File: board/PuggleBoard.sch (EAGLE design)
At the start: 129 parts, among them U1 OPA4209, U10 24C, U2 ADS8331, U3 AD5686, U4 OPA4209, U5 LM2663, U6 TPS7A3001, U7 TPS7A4901, U8 REF5040, U9 AD8032

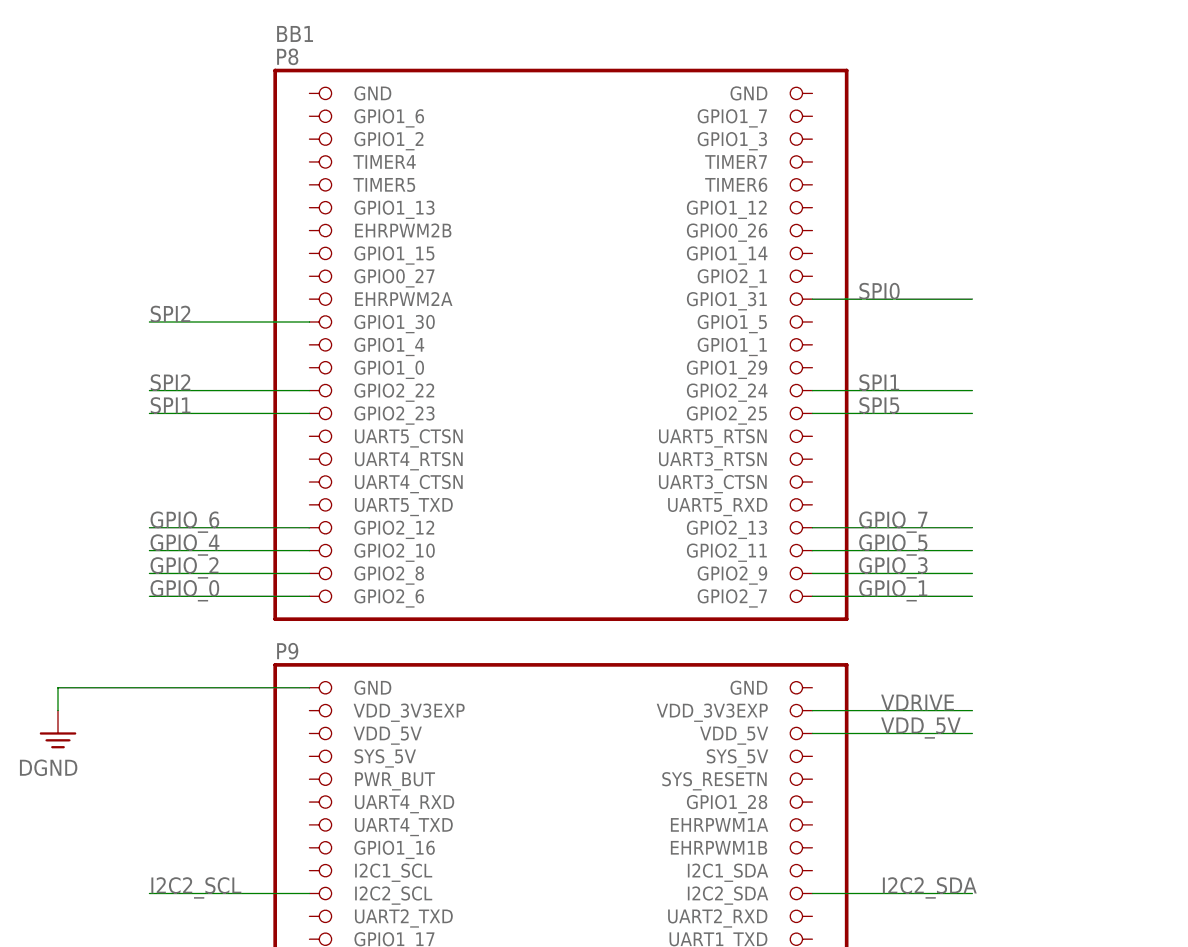
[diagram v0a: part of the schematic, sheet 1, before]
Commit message: Trying to get the positions of the ground planes optimal.
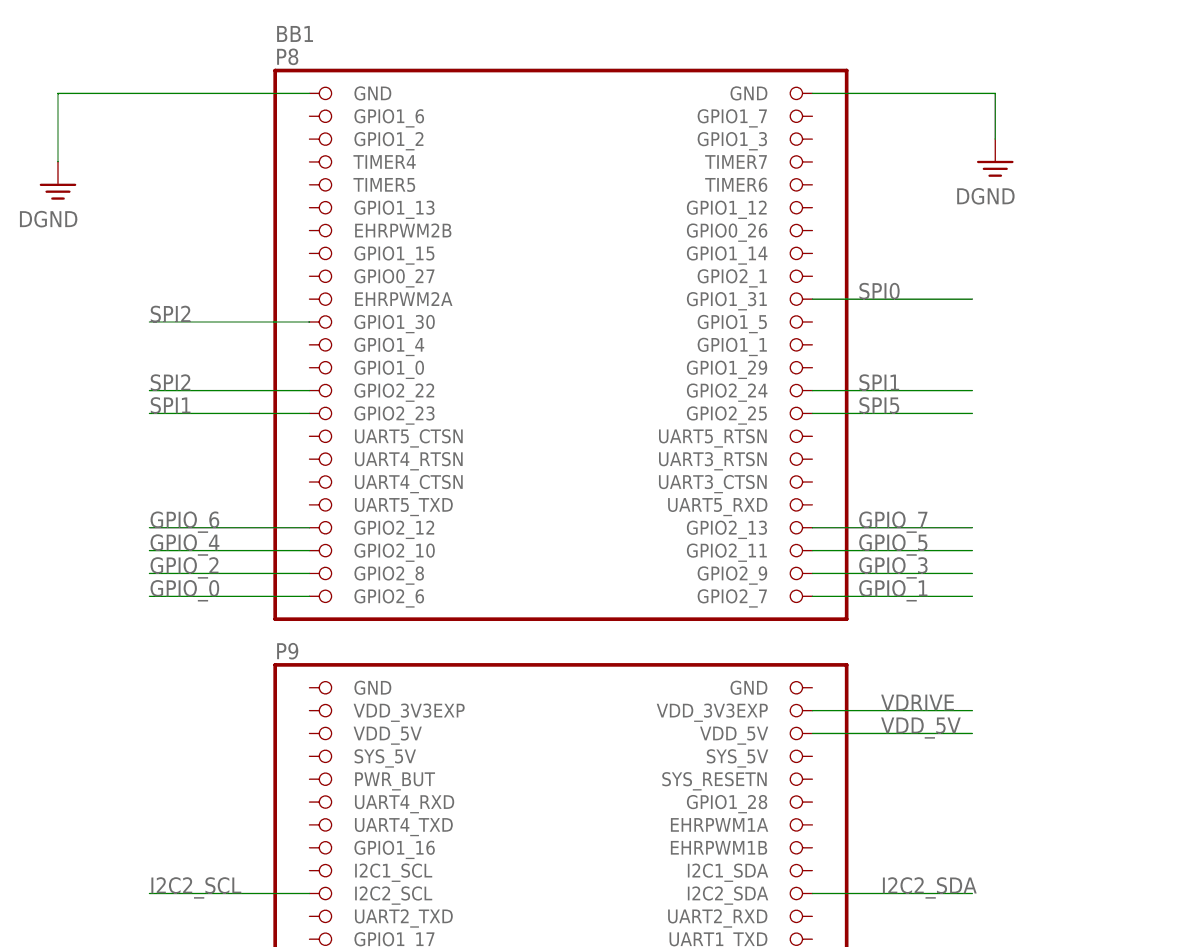
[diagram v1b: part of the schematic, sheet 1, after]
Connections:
- net DGND: now also BB1.GND@7, BB1.GND@8; no longer BB1.GND@1
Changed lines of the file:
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@@
 <part name="C43" library="rcl" deviceset="C-EU" device="C0603" value="0.1uF"/>
 <part name="C44" library="rcl" deviceset="C-EU" device="C0603" value="0.1uF"/>
+<part name="DGND3" library="supply2" deviceset="PE" device="" value="DGND"/>
 </parts>
 <sheets>
@@
 <instances>
 <instance part="BB1" gate="G$1" x="-35.56" y="48.26"/>
-<instance part="DGND2" gate="PE" x="-91.44" y="38.1"/>
+<instance part="DGND2" gate="PE" x="-91.44" y="99.06"/>
 <instance part="A_I/O" gate="G$1" x="53.34" y="50.8"/>
 <instance part="PWR_EXT" gate="A" x="53.34" y="0"/>
@@
 <instance part="DGND10" gate="PE" x="60.96" y="-27.94"/>
 <instance part="A_I/O1" gate="G$1" x="53.34" y="27.94"/>
+<instance part="DGND3" gate="PE" x="12.7" y="101.6"/>
 </instances>
 <busses>
@@
 <segment>
 <pinref part="DGND2" gate="PE" pin="PE"/>
-<wire x1="-91.44" y1="40.64" x2="-91.44" y2="43.18" width="0.1524" layer="91"/>
-<pinref part="BB1" gate="G$1" pin="GND@1"/>
-<wire x1="-91.44" y1="43.18" x2="-63.5" y2="43.18" width="0.1524" layer="91"/>
+<wire x1="-91.44" y1="101.6" x2="-91.44" y2="109.22" width="0.1524" layer="91"/>
+<pinref part="BB1" gate="G$1" pin="GND@7"/>
+<wire x1="-91.44" y1="109.22" x2="-63.5" y2="109.22" width="0.1524" layer="91"/>
 </segment>
 <segment>
@@
 <wire x1="58.42" y1="30.48" x2="73.66" y2="30.48" width="0.1524" layer="91"/>
 <label x="66.04" y="30.48" size="1.778" layer="95"/>
+</segment>
+<segment>
+<pinref part="BB1" gate="G$1" pin="GND@8"/>
+<wire x1="-7.62" y1="109.22" x2="12.7" y2="109.22" width="0.1524" layer="91"/>
+<wire x1="12.7" y1="109.22" x2="12.7" y2="104.14" width="0.1524" layer="91"/>
+<pinref part="DGND3" gate="PE" pin="PE"/>
 </segment>
 </net>
@@
 <wire x1="111.76" y1="-33.02" x2="129.54" y2="-33.02" width="0.1524" layer="91"/>
 <junction x="111.76" y="-33.02"/>
-</segment>
-</net>
+<junction x="129.54" y="-33.02"/>
+</segment>
+</net>

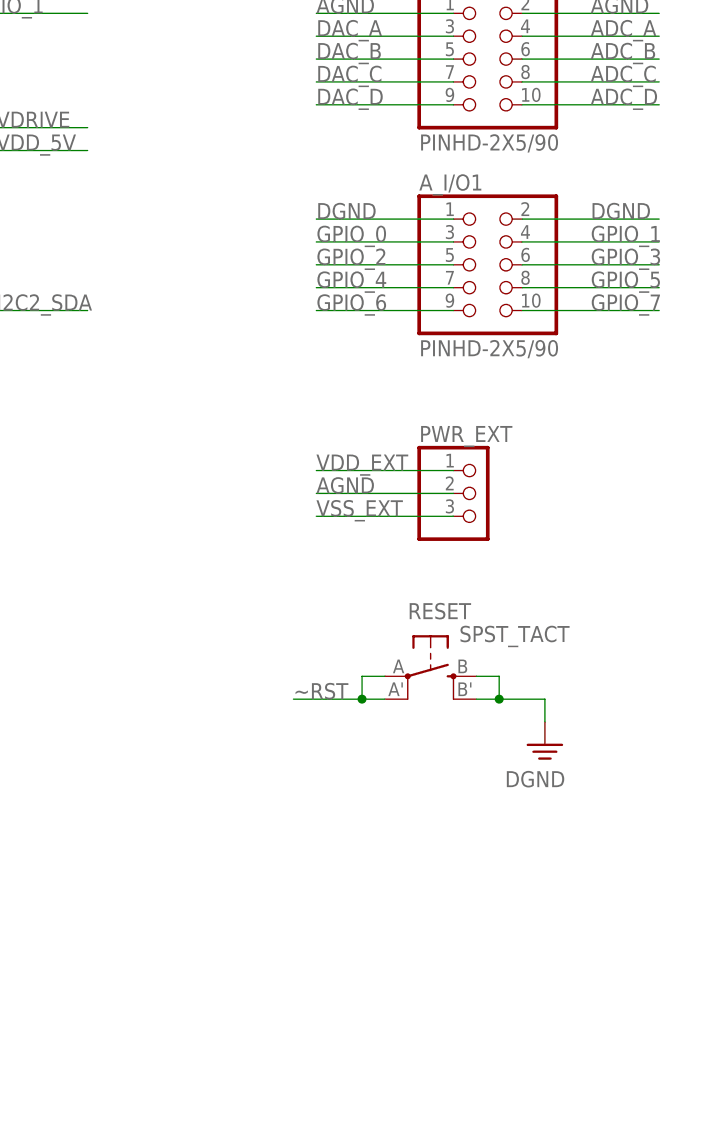
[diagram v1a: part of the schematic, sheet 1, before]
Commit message: Relaced through-hole header for GPIO with HDMI connector. This board will be intan ready.
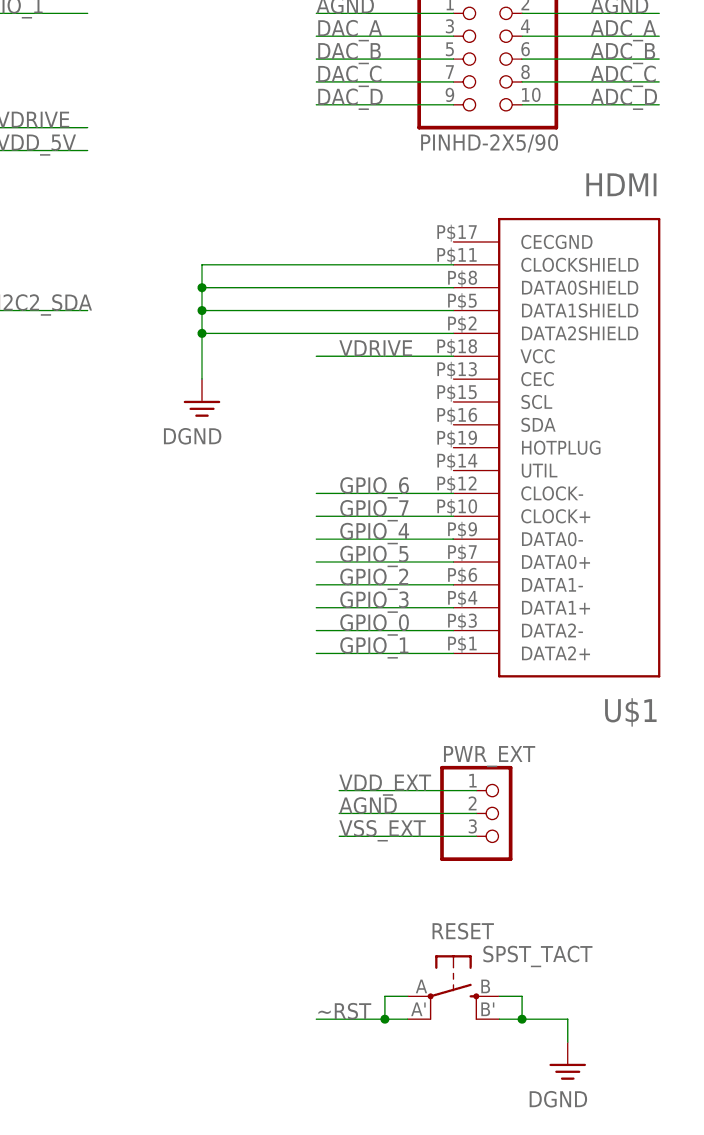
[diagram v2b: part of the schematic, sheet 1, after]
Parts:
- removed A_I/O1: PINHD-2X5/90, adafruit:PINHD-2X5/90
- added U$1: HDMI, open-ephys:HDMI
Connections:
- net DGND: now also U$1.CLOCKSHIELD, U$1.DATA0SHIELD, U$1.DATA1SHIELD, U$1.DATA2SHIELD; no longer A_I/O1.1, A_I/O1.2
- net GPIO_0: now also U$1.DATA2-; no longer A_I/O1.3
- net GPIO_1: now also U$1.DATA2+; no longer A_I/O1.4
- net GPIO_2: now also U$1.DATA1-; no longer A_I/O1.5
- net GPIO_3: now also U$1.DATA1+; no longer A_I/O1.6
- net GPIO_4: now also U$1.DATA0-; no longer A_I/O1.7
- net GPIO_5: now also U$1.DATA0+; no longer A_I/O1.8
- net GPIO_6: now also U$1.CLOCK-; no longer A_I/O1.9
- net GPIO_7: now also U$1.CLOCK+; no longer A_I/O1.10
- net VDRIVE: now also U$1.VCC
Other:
- moved on the sheet: PWR_EXT, RESET

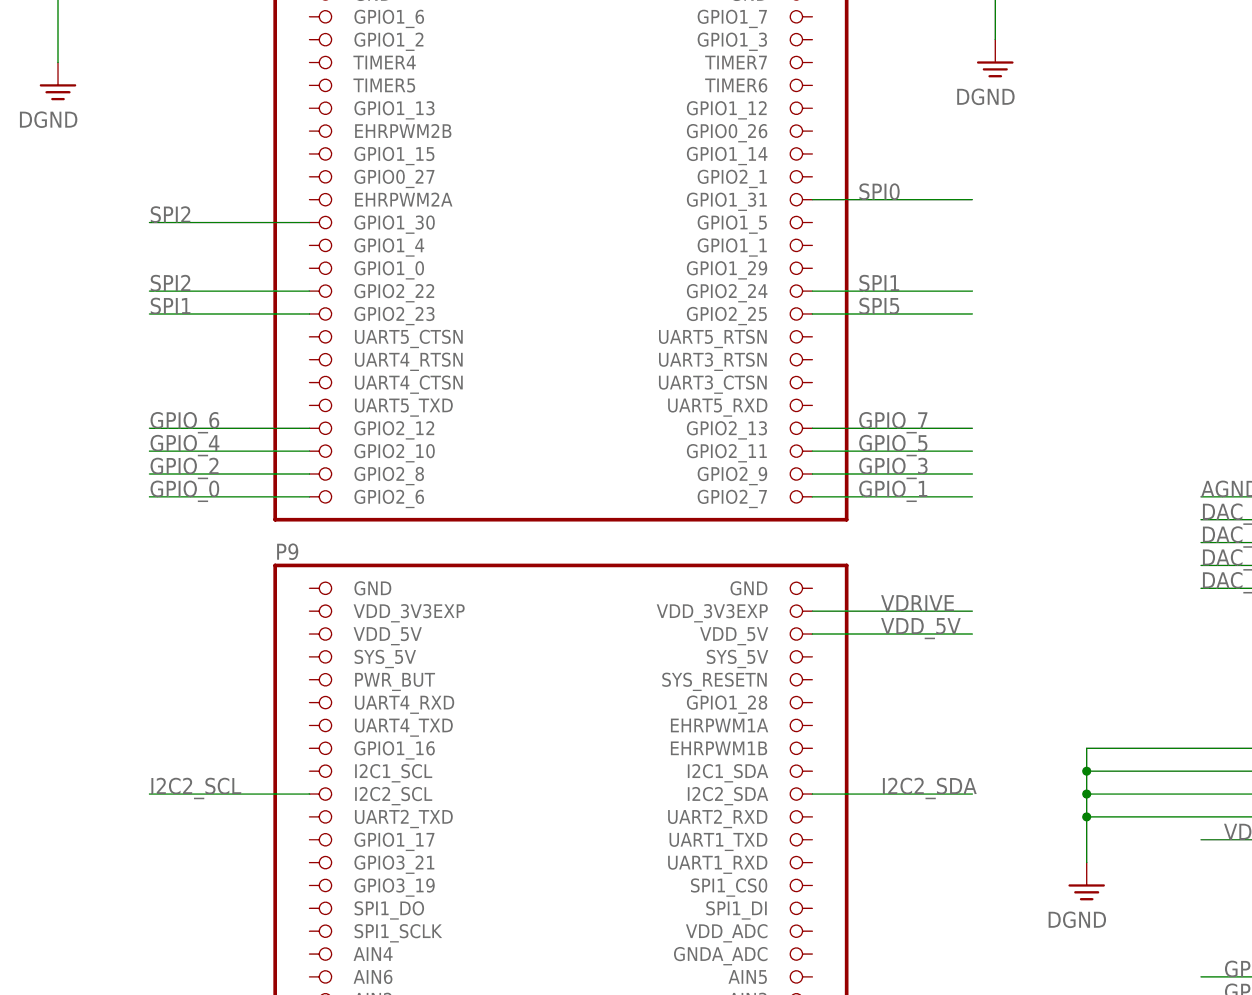
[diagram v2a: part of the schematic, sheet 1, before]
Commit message: Added series resistors to digital I/O lines.
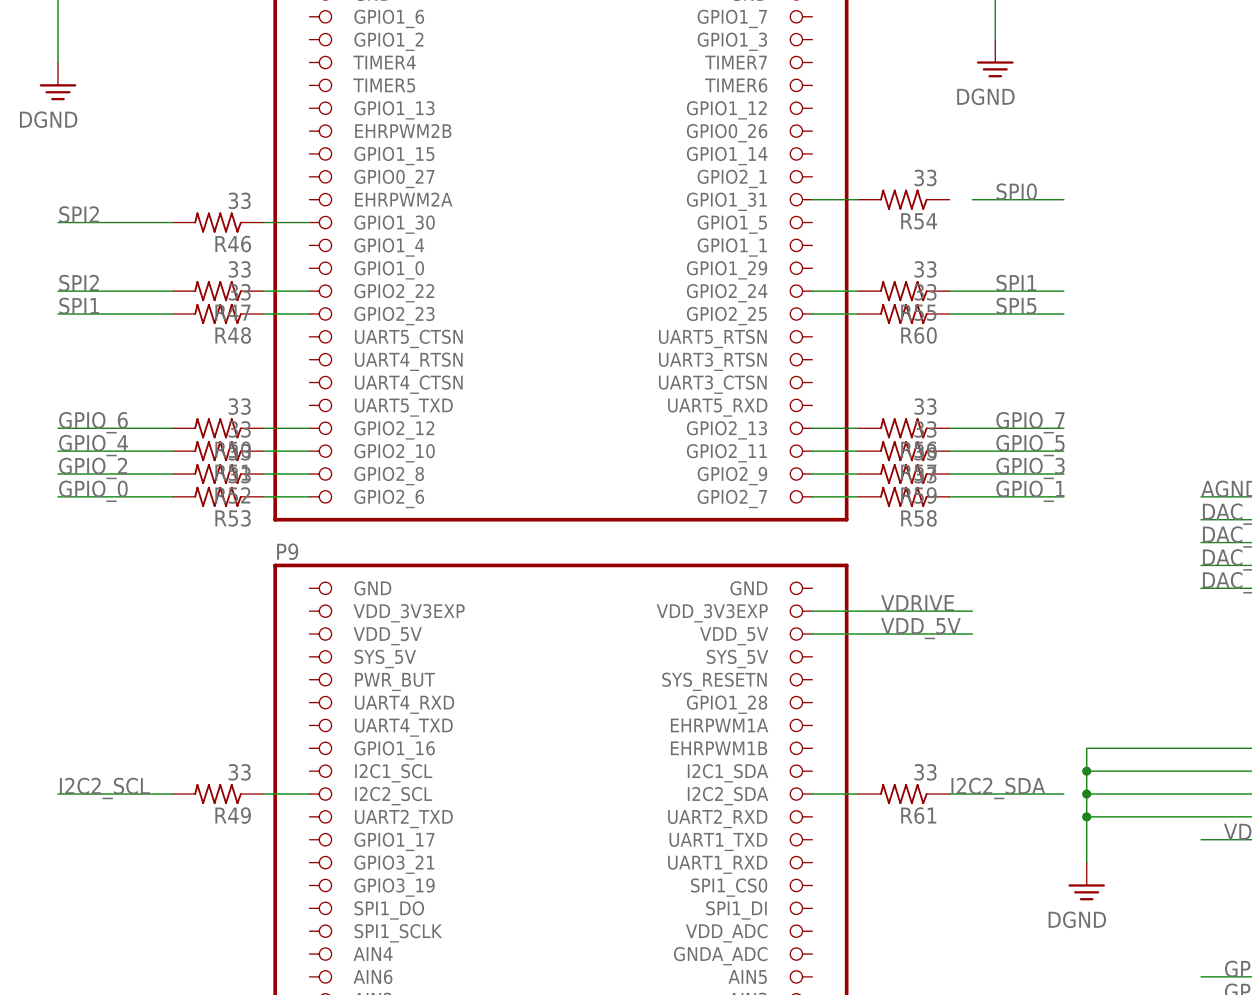
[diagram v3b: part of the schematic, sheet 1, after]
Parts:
- added R46, R47, R48, R49, R50, R51, R52, R53, R54, R55, R56, R57, R58, R59, R60, R61: 33, rcl:R-US_R0603
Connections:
- removed net SPI0: BB1.GPIO1_31, U2.FS/~CS
- removed net SPI3: U2.SDI, U3.SDIN
- removed net SPI4: U2.SDO, U3.SDO
- new net N$10: BB1.GPIO2_24, R55.2
- new net N$12: BB1.GPIO1_31, R54.2
- new net N$13: BB1.GPIO2_13, R56.2
- new net N$15: BB1.GPIO2_11, R57.2
- new net N$17: BB1.GPIO2_9, R59.2
- new net N$21: BB1.GPIO2_7, R58.2
- new net N$23: BB1.GPIO2_6, R53.1
- new net N$25: BB1.GPIO2_8, R52.1
- new net N$26: BB1.GPIO2_10, R51.1
- new net N$27: BB1.GPIO2_12, R50.1
- new net N$28: BB1.GPIO2_23, R48.1
- new net N$29: BB1.GPIO2_22, R47.1
- new net N$30: BB1.GPIO1_30, R46.1
- new net N$31: BB1.I2C2_SCL, R49.1
- new net N$35: BB1.I2C2_SDA, R61.2
- new net N$8: BB1.GPIO2_25, R60.2
- net GPIO_0: now also R53.2; no longer BB1.GPIO2_6
- net GPIO_1: now also R58.1; no longer BB1.GPIO2_7
- net GPIO_2: now also R52.2; no longer BB1.GPIO2_8
- net GPIO_3: now also R59.1; no longer BB1.GPIO2_9
- net GPIO_4: now also R51.2; no longer BB1.GPIO2_10
- net GPIO_5: now also R57.1; no longer BB1.GPIO2_11
- net GPIO_6: now also R50.2; no longer BB1.GPIO2_12
- net GPIO_7: now also R56.1; no longer BB1.GPIO2_13
- net I2C2_SCL: no longer BB1.I2C2_SCL
- net I2C2_SDA: no longer BB1.I2C2_SDA
- net N$24: no longer U2.ADCIN
- net SPI1: now also R48.2, R55.1; no longer BB1.GPIO2_23, BB1.GPIO2_24, U3.SYNC*
- net SPI2: now also R46.2, R47.2; no longer BB1.GPIO1_30, BB1.GPIO2_22, U2.SCLK, U3.SCLK
- net SPI5: now also R60.1; no longer BB1.GPIO2_25, U2.~CONVST
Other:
- moved on the sheet: C12, C13, C14, R19, R22, R25

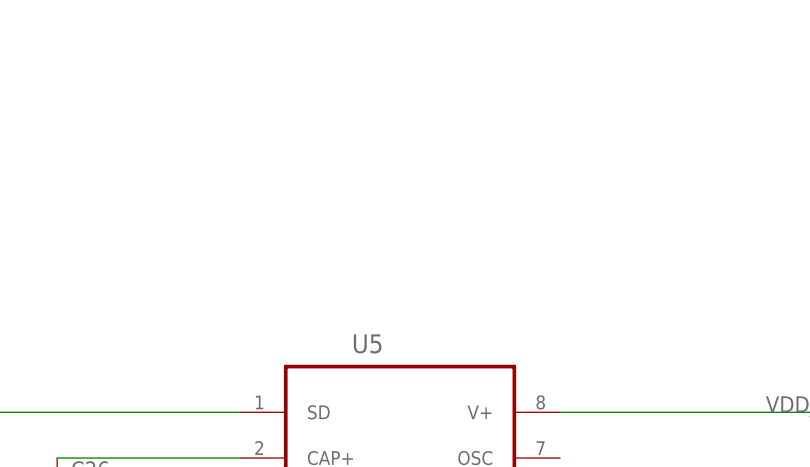
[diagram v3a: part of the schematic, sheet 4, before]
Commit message: Added inverter to design.
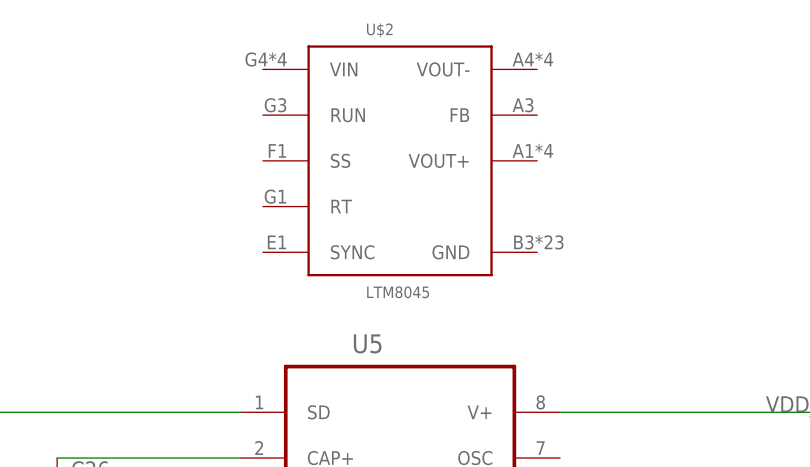
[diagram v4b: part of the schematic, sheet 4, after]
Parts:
- added U$2: LTM8045, boneclamp:LTM8045
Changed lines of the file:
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@@
 <part name="R60" library="rcl" deviceset="R-US_" device="R0603" value="33"/>
 <part name="R61" library="rcl" deviceset="R-US_" device="R0603" value="33"/>
+<part name="U$2" library="boneclamp" deviceset="LTM8045" device=""/>
 </parts>
 <sheets>
@@
 <instance part="C27" gate="G$1" x="-33.02" y="-22.86"/>
 <instance part="SUPPLY27" gate="G$1" x="-33.02" y="-43.18"/>
+<instance part="U$2" gate="G$1" x="2.54" y="71.12"/>
 </instances>
 <busses>
